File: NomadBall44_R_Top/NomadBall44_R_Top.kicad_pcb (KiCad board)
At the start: 2 copper layers, 147.4 x 96.5 mm, 56 parts, among them SW1 SW_Push, SW10 SW_Push, SW11 SW_Push, SW12 SW_Push, SW13 SW_Push, SW14 SW_Push, SW15 SW_Push, SW16 SW_Push, SW17 SW_Push, SW18 SW_Push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

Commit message: スイッチホールとネジ用ホールを設定
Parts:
- REF** (x8): value MountingHole_4.3mm_M4 -> Val**; footprint MountingHole:MountingHole_4.3mm_M4 -> NomadBall44:m2_Screw_Hole
- SW1, SW10, SW11, SW12, SW13, SW14, SW15, SW16, SW17, SW18, SW2, SW22, SW3, SW4, SW5, SW6, SW7, SW8, SW9: footprint NomadBall44:Choc_v2_Hotswap_1u -> NomadBall44:SW_Hole_1u
- SW19, SW20: footprint NomadBall44:Kailh_Choc_V1_Hotswap_thin_via -> NomadBall44:SW_Hole_1u

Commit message: ダイオードを削除
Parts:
- removed D1, D10, D11, D12, D13, D14, D15, D16, D17, D18, D19, D2, D20, D21, D22, D3, D4, D5, D6, D7, D8, D9: D, NomadBall44:Diode_SMD

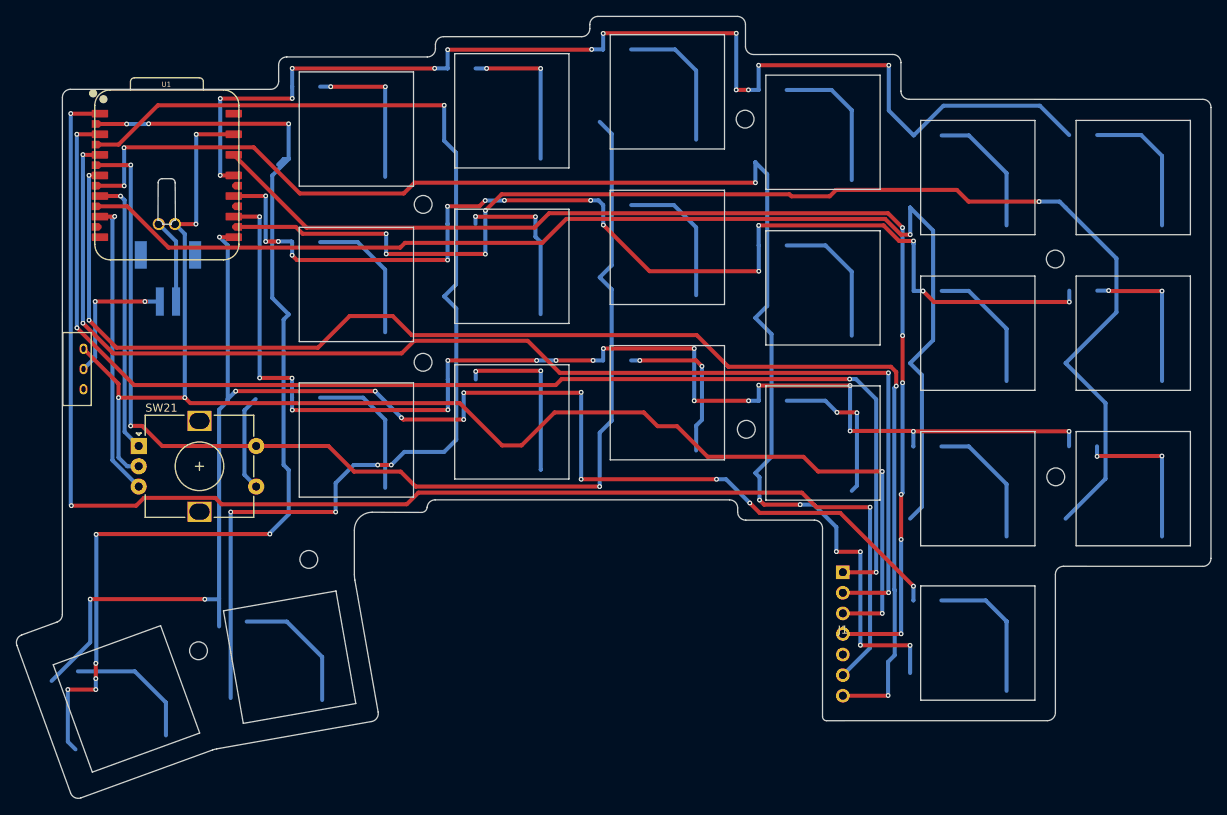
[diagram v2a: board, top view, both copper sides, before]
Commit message: 配線を削除
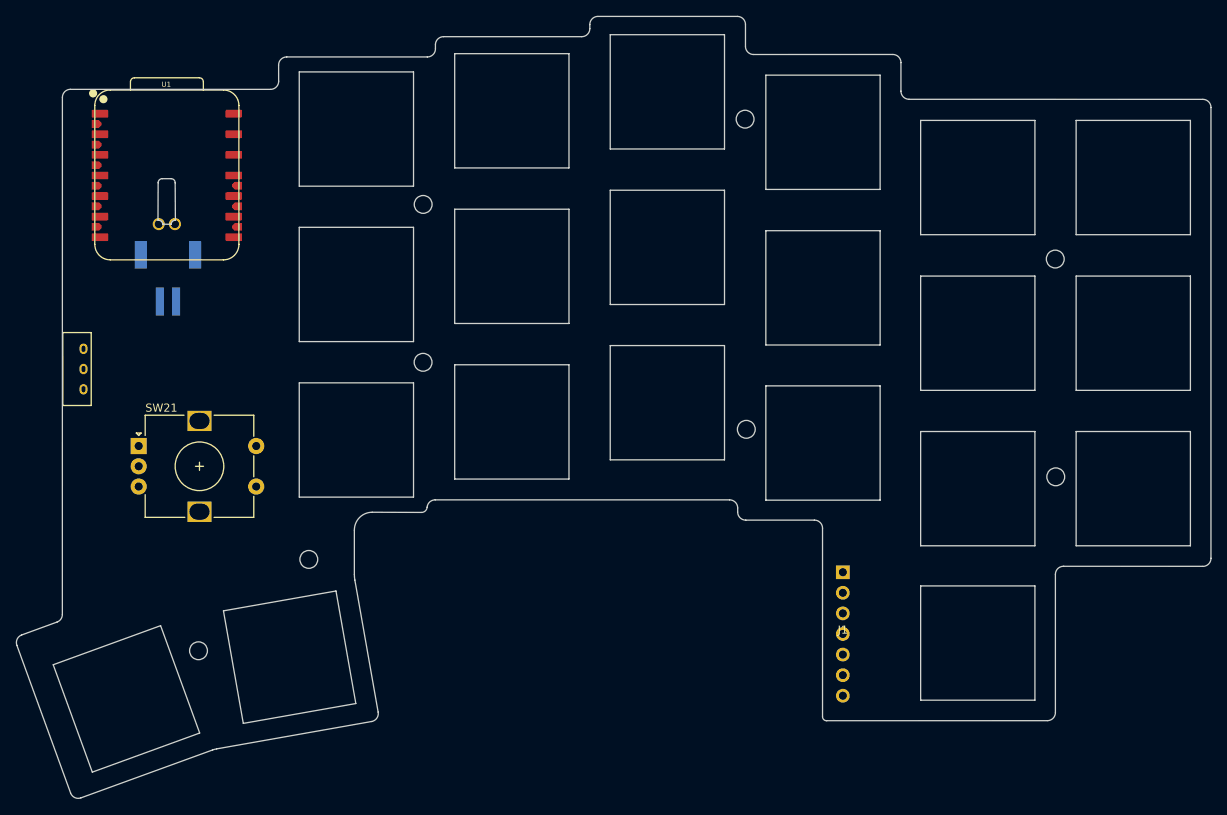
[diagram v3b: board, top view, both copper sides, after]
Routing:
- net Row3: track 186.4 -> 0.00 mm, vias 13 -> 0
- net GND: track 182.4 -> 0.23 mm, vias 6 -> 0
- net SDIO: track 174.7 -> 0.00 mm, vias 3 -> 0
- net Col3: track 174.5 -> 0.37 mm, vias 9 -> 0
- net MOTION: track 170.7 -> 0.00 mm, vias 4 -> 0
- net Col5: track 160.3 -> 0.00 mm, vias 5 -> 0
- net CS: track 158.9 -> 0.00 mm, vias 4 -> 0
- net SCLK: track 155.1 -> 0.01 mm, vias 4 -> 0
- net Row2: track 152.2 -> 0.00 mm, vias 18 -> 0
- net Col4: track 150.0 -> 0.00 mm, vias 1 -> 0
- net 3.3V: track 145.1 -> 0.00 mm, vias 6 -> 0
- net Col2: track 144.8 -> 0.00 mm, vias 3 -> 0
- net Col1: track 144.5 -> 0.00 mm, vias 5 -> 0
- net Row0: track 143.9 -> 0.00 mm, vias 13 -> 0
- net Row1: track 137.2 -> 0.00 mm, vias 15 -> 0
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
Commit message: トッププレートに不要なエリアを削除
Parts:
- removed the REF** at (109.4, 107.7)
- removed the REF** at (95.8, 119.0)
- removed SW19, SW20: SW_Push, NomadBall44:SW_Hole_1u
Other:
- board size 147.4 x 96.5 mm -> 115 x 86.9 mm

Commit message: ネジ穴を一つ追加
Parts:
- added REF**: Val**, NomadBall44:m2_Screw_Hole, F.Cu at (186.3, 108.4)
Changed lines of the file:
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@@
+		(embedded_fonts no)
+	)
+	(footprint "NomadBall44:m2_Screw_Hole"
+		(layer "F.Cu")
+		(at 186.26 108.44)
+		(descr "Mounting Hole 2.2mm, no annular, M2")
+		(tags "mounting hole 2.2mm no annular m2")
+		(property "Reference" "REF**"
+			(at 0 -3.2 0)
+			(layer "F.Fab")
+			(effects
+				(font
+					(size 1 1)
+					(thickness 0.15)
+				)
+			)
+		)
+		(property "Value" "Val**"
+			(at 0 3.2 0)
+			(layer "F.Fab")
+			(effects
+				(font
+					(size 1 1)
+					(thickness 0.15)
+				)
+			)
+		)
+		(property "Datasheet" ""
+			(at 0 0 0)
+			(layer "F.Fab")
+			(hide yes)
+			(effects
+				(font
+					(size 1.27 1.27)
+					(thickness 0.15)
+				)
+			)
+		)
+		(property "Description" ""
+			(at 0 0 0)
+			(layer "F.Fab")
+			(hide yes)
+			(effects
+				(font
+					(size 1.27 1.27)
+					(thickness 0.15)
+				)
+			)
+		)
+		(attr exclude_from_pos_files exclude_from_bom)
+		(fp_circle
+			(center 0 0)
+			(end 2.2 0)
+			(stroke
+				(width 0.15)
+				(type solid)
+			)
+			(fill no)
+			(layer "Cmts.User")
+		)
+		(fp_circle
+			(center 0 0)
+			(end 2.45 0)
+			(stroke
+				(width 0.05)
+				(type solid)
+			)
+			(fill no)
+			(layer "F.CrtYd")
+		)
+		(fp_text user "${REFERENCE}"
+			(at 0.3 0 0)
+			(layer "F.Fab")
+			(effects
+				(font
+					(size 1 1)
+					(thickness 0.15)
+				)
+			)
+		)
+		(pad "" np_thru_hole circle
+			(at 0 0)
+			(size 2.2 2.2)
+			(drill 2.2)
+			(layers "*.Cu" "*.Mask")
+		)
 		(embedded_fonts no)
 	)

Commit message: トッププレートのガーバファイルを生成
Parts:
- removed BT1: Battery_Cell, NomadBall44:JST_S2B-PH-SM4-TB
- removed J1: ~, NomadBall44:pmw3610_connector
- removed SW21: RotaryEncoder_Switch, Rotary_Encoder:RotaryEncoder_Alps_EC12E-Switch_Vertical_H20mm
- removed SW23: SW_SPDT, NomadBall44:TGSW_MSK-12D19
- removed U1: XIAO-nRF52840-Plus-SMD, NomadBall44:XIAO-nRF52840-Plus
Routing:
- net Bat: track 0.95 -> 0.00 mm
